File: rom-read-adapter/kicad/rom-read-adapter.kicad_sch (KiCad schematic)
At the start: 48 parts, among them J1 Host_Conn_02x25, J10 Conn_01x04_Pin, J2 ZIF-48, J3 Conn_01x24_Pin, J4 Conn_01x13_Pin, J5 Conn_01x24_Pin, J6 Conn_01x05_Pin, J7 Conn_01x02_Pin, J8 Conn_01x03_Pin

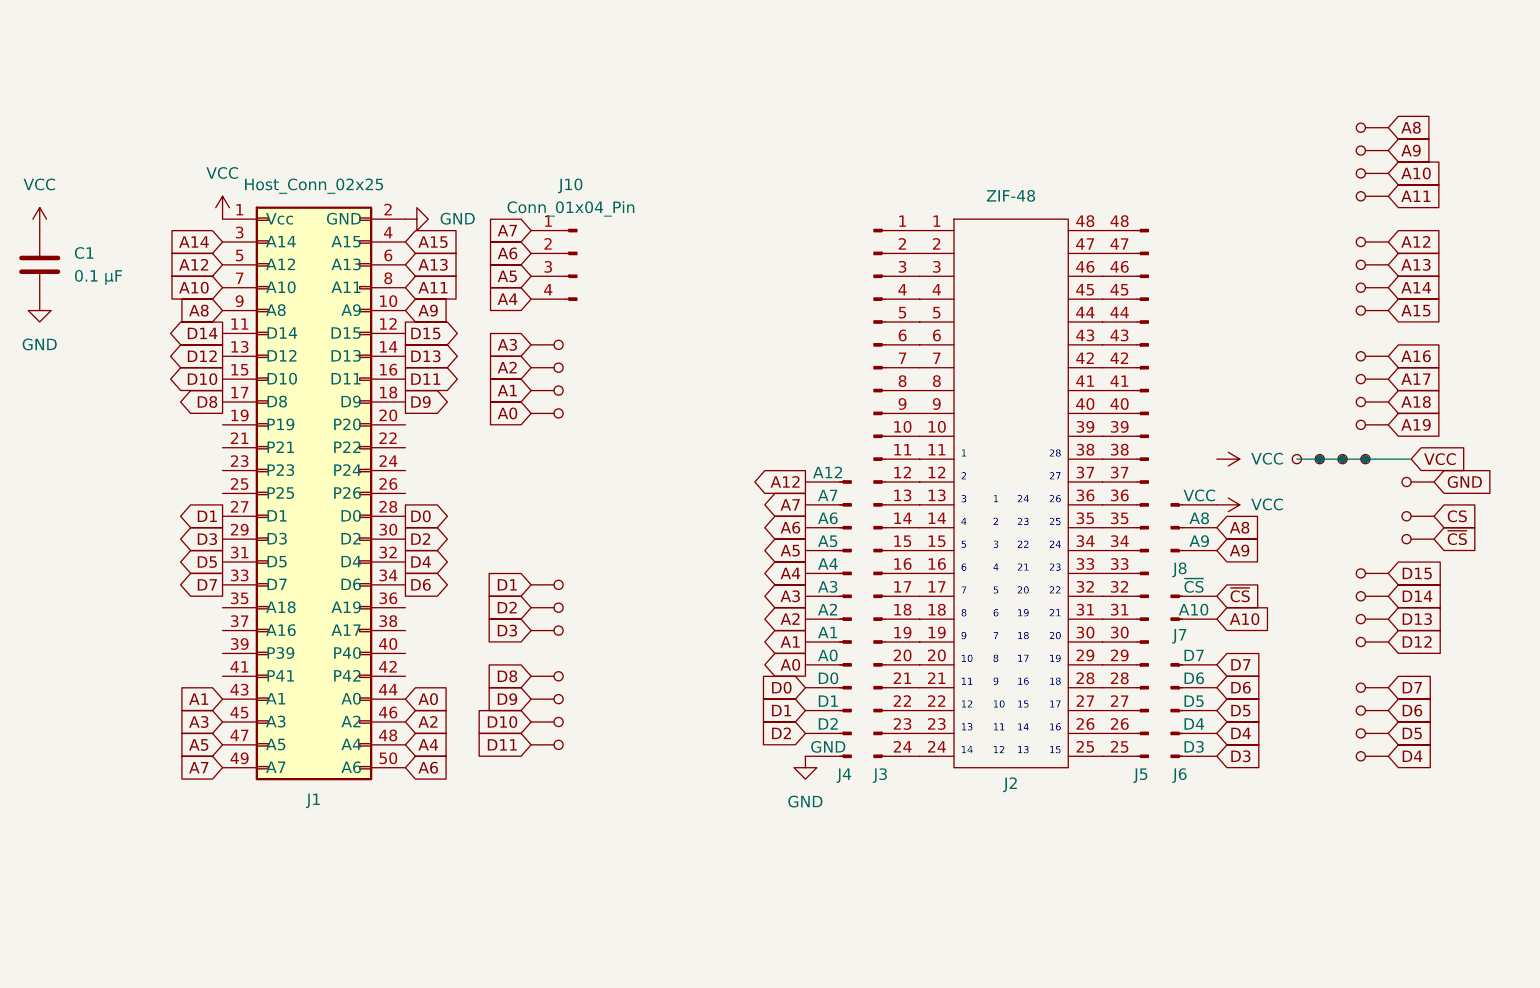
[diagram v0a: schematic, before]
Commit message: WIP rom-read-adapter sch: Completed Schematic
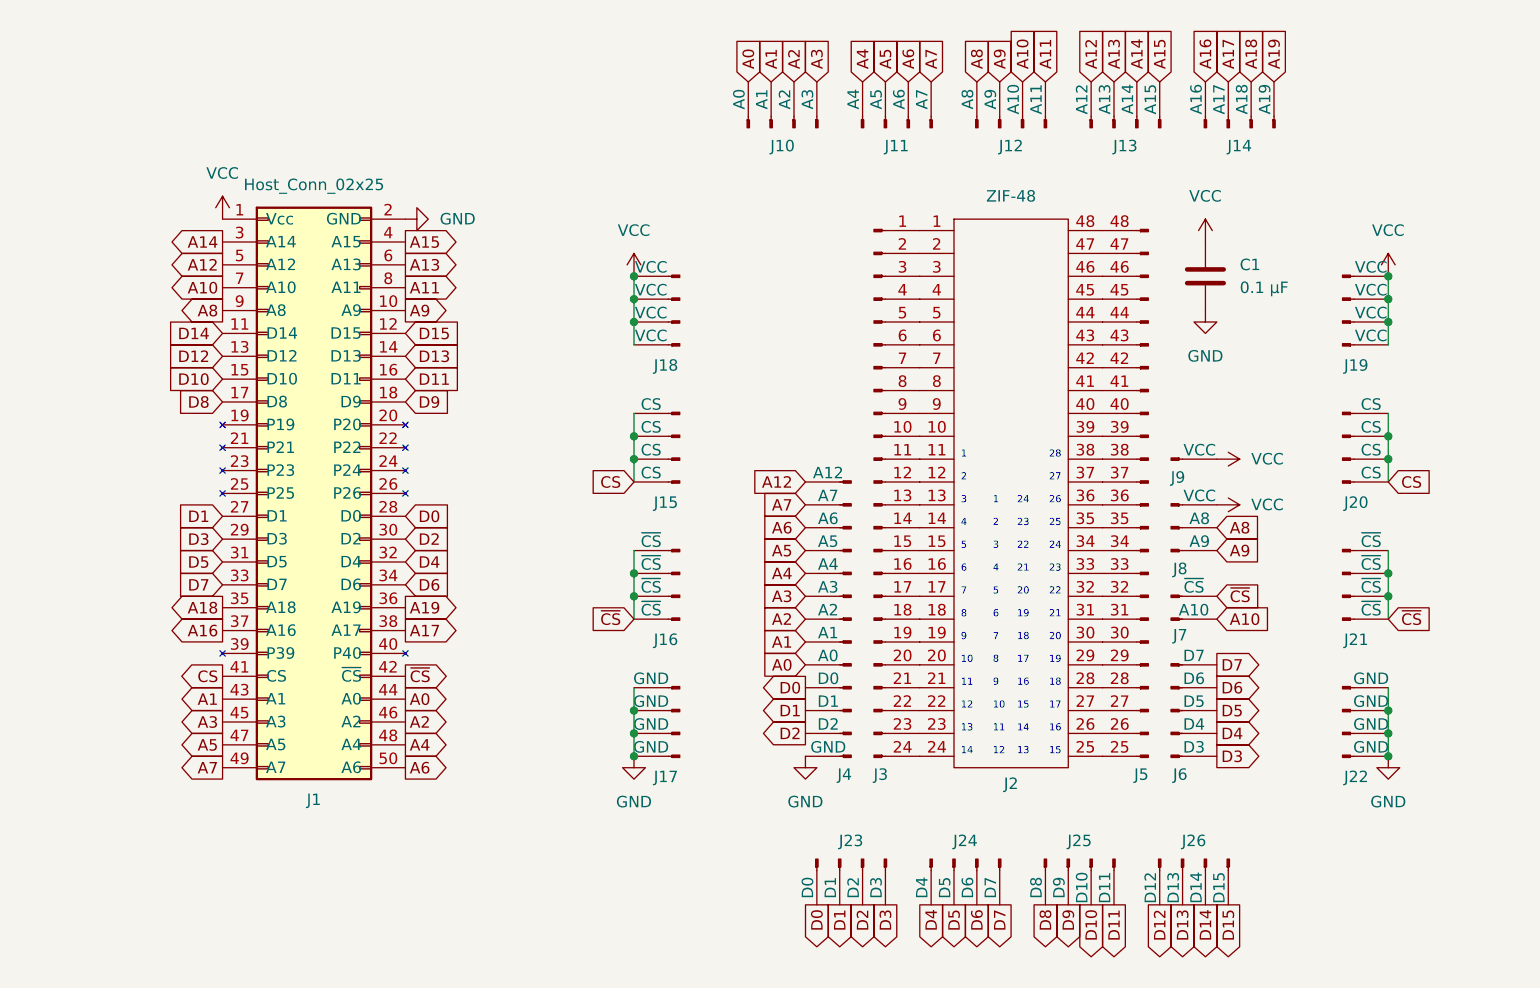
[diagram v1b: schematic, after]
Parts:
- removed JPA1, JPA10, JPA11, JPA12, JPA13, JPA14, JPA15, JPA16, JPA17, JPA18, JPA19, JPA2, JPA20, JPA25, JPA26, JPA27, JPA28, JPA29, JPA3, JPA30, JPA31, JPA32, JPA34, JPA35, JPA36, JPA37, JPA38, JPA39, JPA4, JPA40, JPA41, JPA42, JPA43, JPA5, JPA6, JPA7, JPA8, JPA9: Header_Pin, symbol 0cjs-hwdev:Header_Pin
- added J11, J12, J13, J14, J15, J16, J17, J18, J19, J20, J21, J22, J23, J24, J25, J26: Conn_01x04_Pin, symbol Connector:Conn_01x04_Pin
- added J9: Conn_01x01_Pin, symbol Connector:Conn_01x01_Pin
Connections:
- net A0: now also J10.1 (A0)
- net A1: now also J10.2 (A1)
- net A10: now also J12.3 (A10)
- net A11: now also J12.4 (A11)
- net A12: now also J13.1 (A12)
- net A13: now also J13.2 (A13)
- net A14: now also J13.3 (A14)
- net A15: now also J13.4 (A15)
- net A16: now also J1.37 (A16), J14.1 (A16)
- net A17: now also J1.38 (A17), J14.2 (A17)
- net A18: now also J1.35 (A18), J14.3 (A18)
- net A19: now also J1.36 (A19), J14.4 (A19)
- net A2: now also J10.3 (A2)
- net A3: now also J10.4 (A3)
- net A4: now also J11.1 (A4); no longer J10.4 (Pin_4)
- net A5: now also J11.2 (A5); no longer J10.3 (Pin_3)
- net A6: now also J11.3 (A6); no longer J10.2 (Pin_2)
- net A7: now also J11.4 (A7); no longer J10.1 (Pin_1)
- net A8: now also J12.1 (A8)
- net A9: now also J12.2 (A9)
- net CS: now also J1.41 (CS), J15.1 (CS), J15.2 (CS), J15.3 (CS), J15.4 (CS), J20.1 (CS), J20.2 (CS), J20.3 (CS), J20.4 (CS)
- net D0: now also J23.1 (D0)
- net D1: now also J23.2 (D1)
- net D10: now also J25.3 (D10)
- net D11: now also J25.4 (D11)
- net D12: now also J26.1 (D12)
- net D13: now also J26.2 (D13)
- net D14: now also J26.3 (D14)
- net D15: now also J26.4 (D15)
- net D2: now also J23.3 (D2)
- net D3: now also J23.4 (D3)
- net D4: now also J24.1 (D4)
- net D5: now also J24.2 (D5)
- net D6: now also J24.3 (D6)
- net D7: now also J24.4 (D7)
- net D8: now also J25.1 (D8)
- net D9: now also J25.2 (D9)
- net GND: now also J17.1 (GND), J17.2 (GND), J17.3 (GND), J17.4 (GND), J22.1 (GND), J22.2 (GND), J22.3 (GND), J22.4 (GND)
- net VCC: now also J18.1 (VCC), J18.2 (VCC), J18.3 (VCC), J18.4 (VCC), J19.1 (VCC), J19.2 (VCC), J19.3 (VCC), J19.4 (VCC), J9.1 (VCC)
- net ~{CS}: now also J1.42 (~{CS}), J16.1 (~{CS}), J16.2 (~{CS}), J16.3 (~{CS}), J16.4 (~{CS}), J21.1 (~{CS}), J21.2 (~{CS}), J21.3 (~{CS}), J21.4 (~{CS})
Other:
- moved on the sheet: C1
